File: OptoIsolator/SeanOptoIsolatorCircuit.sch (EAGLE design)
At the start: 10 parts, among them Q1 BROADCOM_HCNR200-300EBROADCOM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, U1 MCP6002-E/SNSOIC8-N_MC-L, U2 MCP6002-E/SNSOIC8-N_MC-L

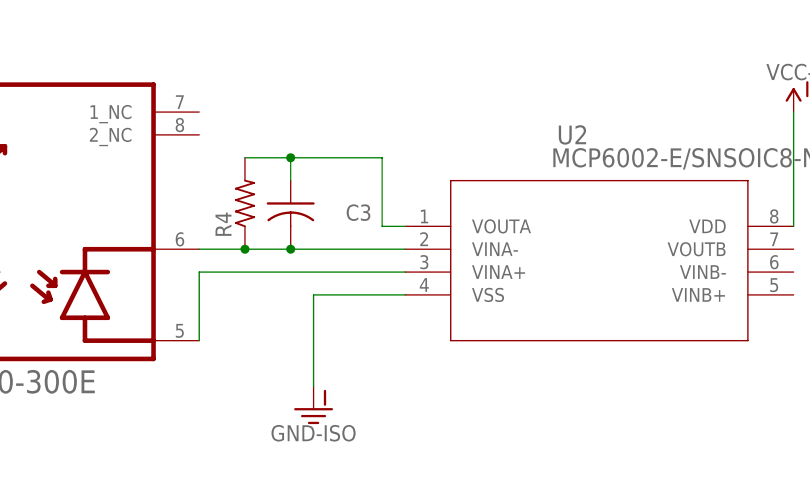
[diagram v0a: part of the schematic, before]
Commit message: made changes to eda schematic and board files. fixing the issues preventing the V0 to work correctly
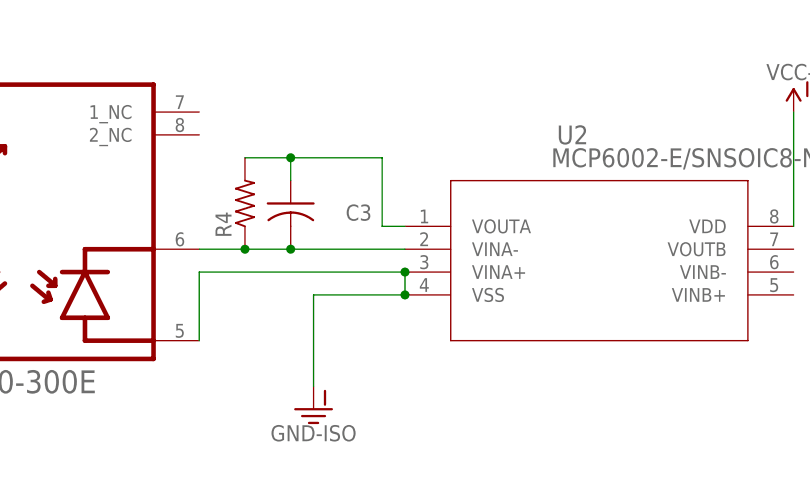
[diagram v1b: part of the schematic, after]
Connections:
- removed net N$6: Q1.PD2_ANODE, U2.VINA+
- net GND-ISO: now also Q1.PD2_ANODE, U2.VINA+
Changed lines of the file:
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@@
-</segment>
-</net>
-<net name="N$6" class="0">
-<segment>
-<pinref part="Q1" gate="G$0" pin="PD2_ANODE"/>
-<pinref part="U2" gate="A" pin="VINA+"/>
-<wire x1="114.3" y1="5.08" x2="114.3" y2="12.7" width="0.1524" layer="91"/>
-<wire x1="114.3" y1="12.7" x2="137.16" y2="12.7" width="0.1524" layer="91"/>
 </segment>
 </net>
@@
 <wire x1="127" y1="10.16" x2="127" y2="0" width="0.1524" layer="91"/>
 <pinref part="GND-ISO1" gate="G$1" pin="GND-ISO"/>
+<pinref part="Q1" gate="G$0" pin="PD2_ANODE"/>
+<pinref part="U2" gate="A" pin="VINA+"/>
+<wire x1="114.3" y1="5.08" x2="114.3" y2="12.7" width="0.1524" layer="91"/>
+<wire x1="114.3" y1="12.7" x2="137.16" y2="12.7" width="0.1524" layer="91"/>
+<wire x1="137.16" y1="10.16" x2="137.16" y2="12.7" width="0.1524" layer="91"/>
+<junction x="137.16" y="10.16"/>
+<junction x="137.16" y="12.7"/>
 </segment>
 </net>
